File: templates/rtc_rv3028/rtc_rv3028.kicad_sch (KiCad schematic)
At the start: 5 parts, among them U8 RV-3028-C7

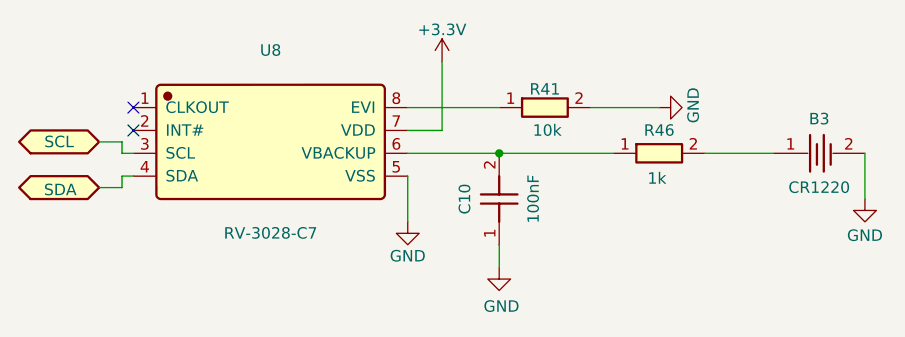
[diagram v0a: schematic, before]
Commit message: Add PCB layout with functional block placement and antenna cutout
4"x4" board with ESP32-S3 antenna at bottom edge (180° rotation),
20x6mm PCB cutout underneath per Espressif specs. Components grouped
by schematic block: PSU chain across top (12V→5V→3.3V), connectors
at top edge, SD card at right edge, flash/RTC/audio grouped near
their bus connections. GND copper pour on both layers. 4x M6 mounting
holes inset 3/8" from edges. Includes JLCImport footprints, 3D models,
patches, and schematic/template updates.

Co-Authored-By: Claude Opus 4.6 <noreply@anthropic.com>
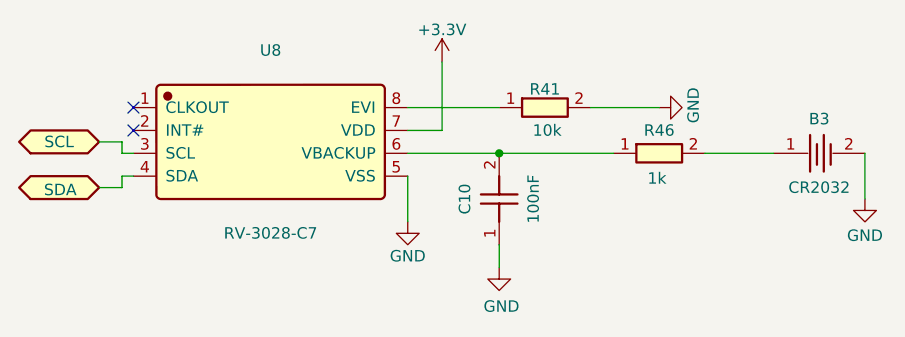
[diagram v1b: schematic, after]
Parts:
- B3: value CR1220 -> CR2032
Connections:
- net SCL: now reaches U8.3 (SCL)
- net SDA: now reaches U8.4 (SDA)
